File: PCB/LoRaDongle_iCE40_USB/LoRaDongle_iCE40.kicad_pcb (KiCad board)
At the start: 4 copper layers, 95 x 67 mm, 137 parts, among them IC1 93LC56BT-I_OT, IC2 ICE40UP5K-UWG30ITR1K, IC3 SGP40-D-R4, J1 USB_A, J2 Conn_01x08, J3 Conn_01x08_Male, J4 Conn_01x04_Male, J5 142-0701-801, J6 Conn_02x02_Top_Bottom, J7 Conn_01x03_Male, J8 Jumper_2_Open, SW1 SW_Push, SW2 SW_Push, U1 RP550K001A-TR, U2 FT2232HL, U3 SX1261IMLTRT, U4 SKY13587-378LF, U5 W25Q128JVS, X1 ECS-2520MV-500-BL-TR, Y1 Crystal_GND24_Small, Y2 Crystal_GND24

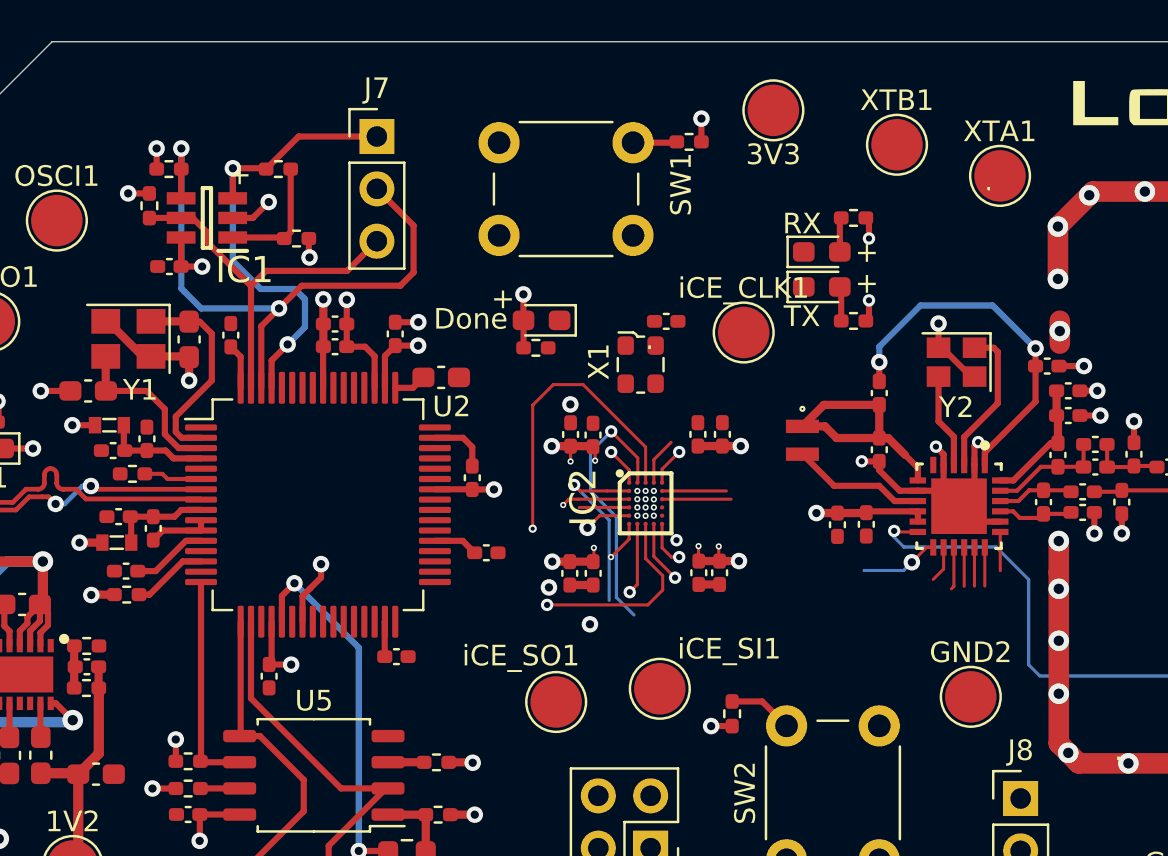
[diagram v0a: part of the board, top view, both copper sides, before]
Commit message: updated schematic to QFN ice40
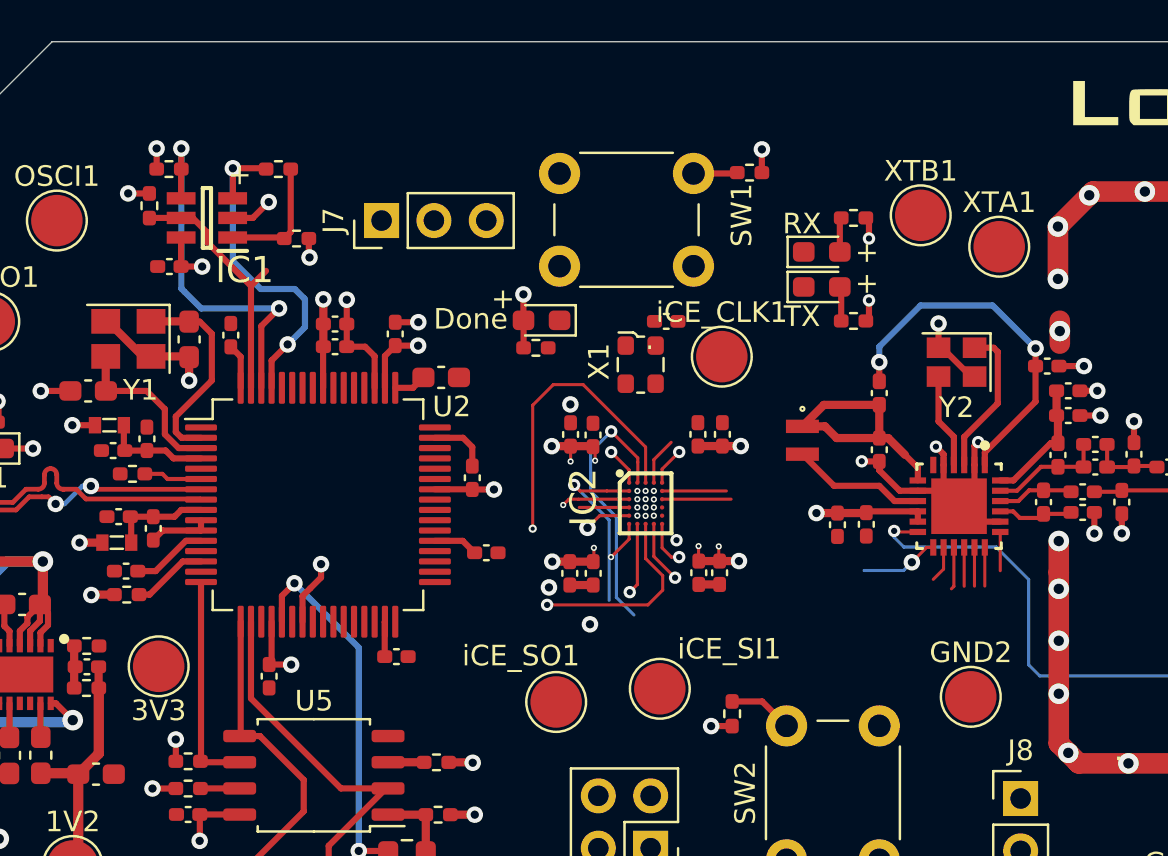
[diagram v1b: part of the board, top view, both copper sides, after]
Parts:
- moved 3V3 40.2 mm to (120.2, 105.3)
- moved J7 4.08 mm to (131.0, 83.7), turned to 90 degrees
- moved XTB1 3.61 mm to (157.2, 83.4)
- moved XTA1 3.44 mm to (161.0, 84.9)
- moved R13 3.29 mm to (148.8, 81.4)
- moved SW1 3.29 mm to (139.6, 81.4)
- moved iCE_CLK1 1.58 mm to (147.5, 90.3)
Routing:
- net /USB_Interface/CLK: track 30.6 -> 18.6 mm
- net /USB_Interface/DATA: track 22.9 -> 16.8 mm
- net Net-(IC1-Pad5): track 18.5 -> 12.6 mm

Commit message: updated routing
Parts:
- removed IC2: ICE40UP5K-UWG30ITR1K, ICE40UP5K-UWG30ITR1K_KiCad:BGA30C40P5X6_211X254X60
- added C56: 1uF, Capacitor_SMD:C_0402_1005Metric_Pad0.74x0.62mm_HandSolder, F.Cu at (137.5, 95.2)
- added C57: 100nF, Capacitor_SMD:C_0402_1005Metric_Pad0.74x0.62mm_HandSolder, F.Cu at (150.9, 97.3)
- added J9: Conn_01x17_Male, Connector_PinHeader_2.54mm:PinHeader_1x17_P2.54mm_Vertical, F.Cu at (118.1, 77.6)
- added U6: ICE40UP5K-SG48ITR, Package_DFN_QFN:QFN-48-1EP_7x7mm_P0.5mm_EP5.6x5.6mm, F.Cu at (143.8, 97.2)
- J2: value Conn_01x08 -> Conn_01x10_Male; footprint Connector_PinHeader_2.54mm:PinHeader_2x04_P2.54mm_Vertical -> Connector_PinHeader_2.54mm:PinHeader_2x05_P2.54mm_Vertical
- R12: value 4K7 -> 2k2
- moved iCE_SI1 25.4 mm to (121.0, 116.1)
- moved D2 17.9 mm to (140.3, 106.4)
- moved R12 17.9 mm to (140.0, 107.7)
- moved C26 13.7 mm to (148.7, 90.1), turned to -90 degrees
- moved iCE_CLK1 10.8 mm to (137.0, 87.6)
- moved C25 10.1 mm to (139.9, 90.8), turned to -90 degrees
- moved iCE_SO1 9.92 mm to (138.1, 116.9)
- moved C31 6.42 mm to (150.9, 99.5), turned to 180 degrees
- moved C30 6.26 mm to (150.9, 98.3), turned to 180 degrees
- moved XTA1 3.75 mm to (162.2, 81.4)
- moved C29 3.72 mm to (137.5, 94.2), turned to 180 degrees
- moved XTB1 2.85 mm to (159.5, 85.0)
- moved C28 2.79 mm to (137.6, 93.1), turned to 180 degrees
- moved R20 2.75 mm to (155.8, 86.6)
- moved R21 2.75 mm to (155.8, 81.6)
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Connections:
- net Net-(IC1-Pad5) renamed /USB_Interface/CS#
- net Net-(R14-Pad2) renamed /ice40up5k_circuit/FLASH_~{WP}
- net Net-(R16-Pad2) renamed /ice40up5k_circuit/FLASH_~{HOLD}
- J2 pad 6: GND -> /SPI_SS
- J2 pad 7: /SPI_SS -> /UART_RX
- J2 pad 8: +5V -> /UART_TX
- U2 pad 38: /USB_Interface/UART_USB_TX -> /UART_RX
- U2 pad 39: /USB_Interface/UART_USB_RX -> /UART_TX
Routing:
- net 1V2FPGA: track 12.2 -> 70.2 mm, vias 6 -> 2
- net /ice40up5k_circuit/Pin16: track 0.00 -> 49.2 mm, vias 0 -> 1
- net 3V3FPGA: track 34.3 -> 82.1 mm, vias 9 -> 3
- net /ice40up5k_circuit/Pin3: track 0.00 -> 40.1 mm, vias 0 -> 1
- net /ice40up5k_circuit/Pin2: track 0.00 -> 39.4 mm, vias 0 -> 1
- net /ice40up5k_circuit/Pin1: track 0.00 -> 38.6 mm, vias 0 -> 1
- net /ice40up5k_circuit/i2C_SDA: track 4.37 -> 40.4 mm
- net /ice40up5k_circuit/Pin15: track 0.00 -> 34.1 mm, vias 0 -> 1
- net /RF Circuitry/ANT_SW: track 2.31 -> 35.7 mm, vias 0 -> 2
- net /ice40up5k_circuit/Pin17: track 0.00 -> 33.0 mm, vias 0 -> 1
- net /ice40up5k_circuit/Pin14: track 0.00 -> 31.6 mm, vias 0 -> 1
- net 1V2: track 12.0 -> 43.0 mm
- net /ice40up5k_circuit/i2C_SCL: track 4.30 -> 34.1 mm
- net /ice40up5k_circuit/iCE_SI: track 2.26 -> 29.2 mm, vias 1 -> 2
- net /ice40up5k_circuit/iCE_SO: track 3.37 -> 30.1 mm
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
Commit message: routing complete
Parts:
- added 5V1: 5V, TestPoint:TestPoint_Pad_D2.5mm, F.Cu at (106.6, 108.1)
- moved GND1 32.1 mm to (139.2, 126.1)
- moved G3 2.99 mm to (176.1, 117.1)
- moved G2 1.25 mm to (186.2, 117.0)
- moved 3V3 0.15 mm to (120.0, 105.3)
- moved C41 0.14 mm to (176.8, 92.9)
- moved C43 0.14 mm to (176.8, 99.3)
- moved CTL2 0.09 mm to (175.6, 112.4)
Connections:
- J3 pad 5: /RF Circuitry/BUSY -> /RF Circuitry/ANT_SW
- J3 pad 7: /RF Circuitry/DIO1 -> /RF Circuitry/BUSY
- J3 pad 8: /RF Circuitry/ANT_SW -> /RF Circuitry/DIO1
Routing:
- net +5V: track 32.9 -> 100.1 mm
- net /ICE_CRESET: track 17.7 -> 80.8 mm, vias 2 -> 5
- net /RF Circuitry/ANT_SW: track 35.7 -> 85.1 mm, vias 2 -> 3
- net /UART_TX: track 7.53 -> 55.7 mm
- net /RF Circuitry/DIO1: track 15.8 -> 62.8 mm, vias 2 -> 3
- net /RF Circuitry/BUSY: track 15.3 -> 58.0 mm
- net /RF Circuitry/~{RESET}: track 15.6 -> 57.4 mm, vias 2 -> 3
- net /UART_RX: track 7.48 -> 48.6 mm, vias 0 -> 4
- net /RF Circuitry/LoRa_!SS: track 19.9 -> 57.0 mm, vias 0 -> 1
- net /RF Circuitry/LoRa_MOSI: track 15.9 -> 51.4 mm, vias 0 -> 2
- net /RF Circuitry/LoRa_MISO: track 15.2 -> 50.0 mm, vias 0 -> 1
- net /ICE_CDONE: track 28.1 -> 61.3 mm, vias 3 -> 6
- net /RF Circuitry/LoRa_SCK: track 16.8 -> 49.4 mm, vias 0 -> 1
- net 1V8: track 7.53 -> 38.6 mm
- net /SPI_SCK: track 34.6 -> 65.2 mm, vias 2 -> 3
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- added copper zone on In2.Cu, net 3V3
- added copper zone on B.Cu, net GND
- added copper zone on F.Cu, net GND
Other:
- board text added: "CPU_RESET"
- board text added: "FTDI EEPROM"
- board text added: "Gas Sensor"
- board text added: "LoRa Connector"
- board text added: "PWR"
- board text added: "RESET"
- board text removed: "FLASH"
- board text removed: "FPGA"
- board text removed: "GND"
- board text removed: "OSC"
- board text removed: "Vin"

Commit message: updated BOM
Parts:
- removed G2: LOGO, Logo:rev1.0
- added G***: LOGO, Logo:rev2, F.Cu at (186.2, 117.0)

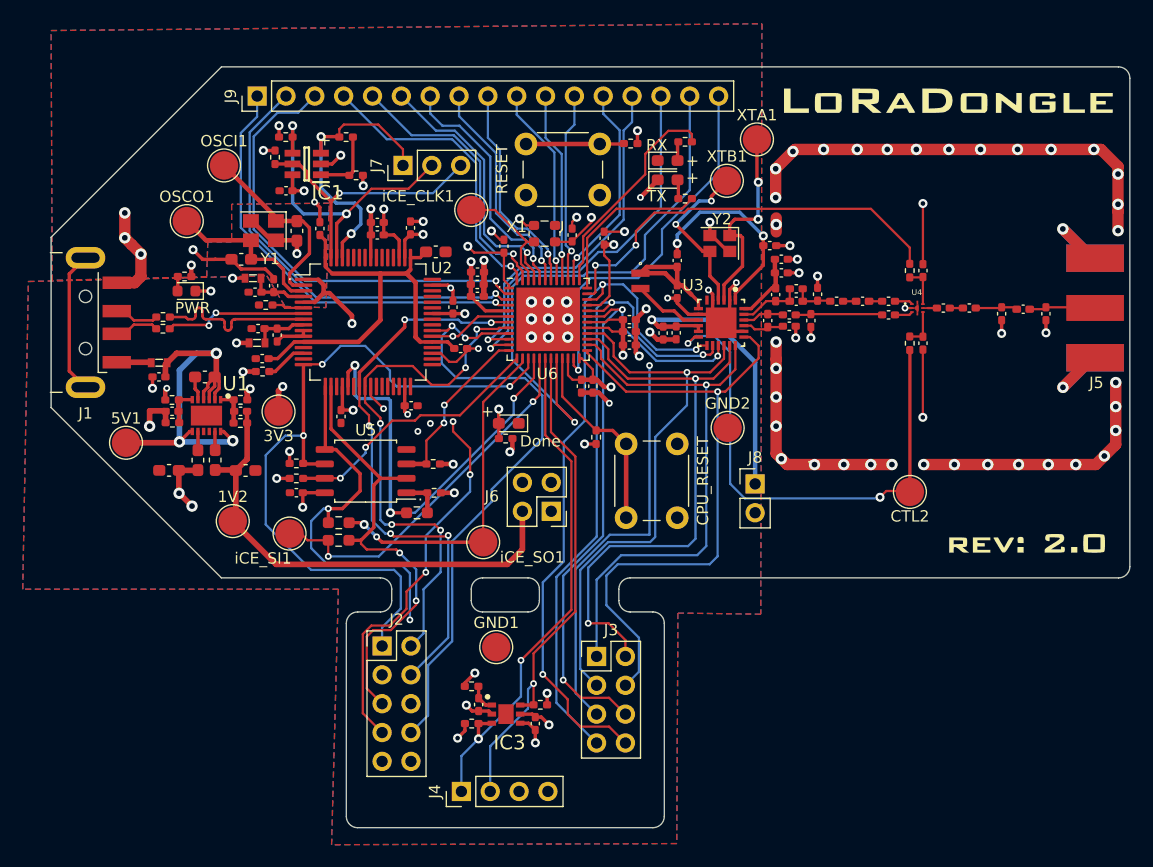
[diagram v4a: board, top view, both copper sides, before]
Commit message: updated silkscreen
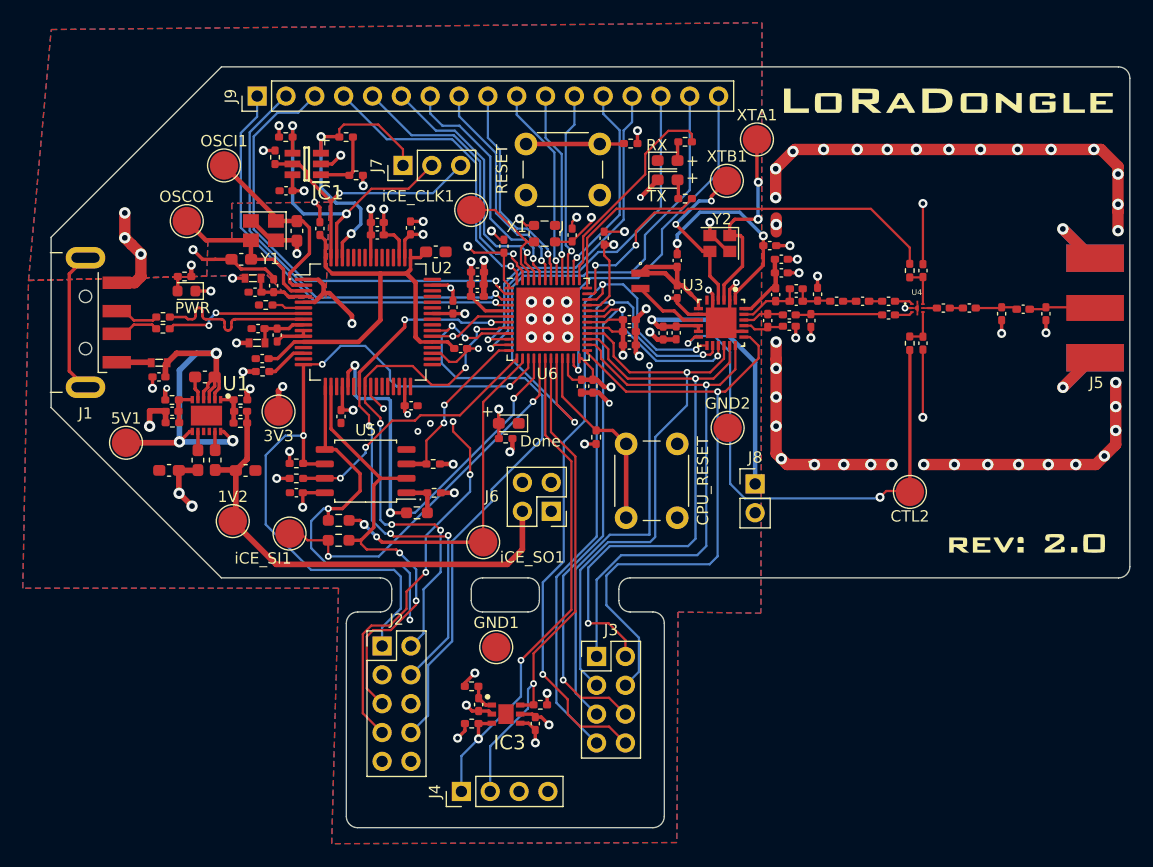
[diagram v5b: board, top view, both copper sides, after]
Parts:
- added G***: LOGO, Logo:qr_code, B.Cu at (176.5, 89.5)
- added REF**: KiCad-Logo2_5mm_SilkScreen, Symbol:KiCad-Logo2_5mm_SilkScreen, B.Cu at (182.5, 104.6)
- added REF**: OSHW-Logo2_9.8x8mm_SilkScreen, Symbol:OSHW-Logo2_9.8x8mm_SilkScreen, B.Cu at (169.2, 104.5)
- moved JP2 0.20 mm to (125.3, 114.9)

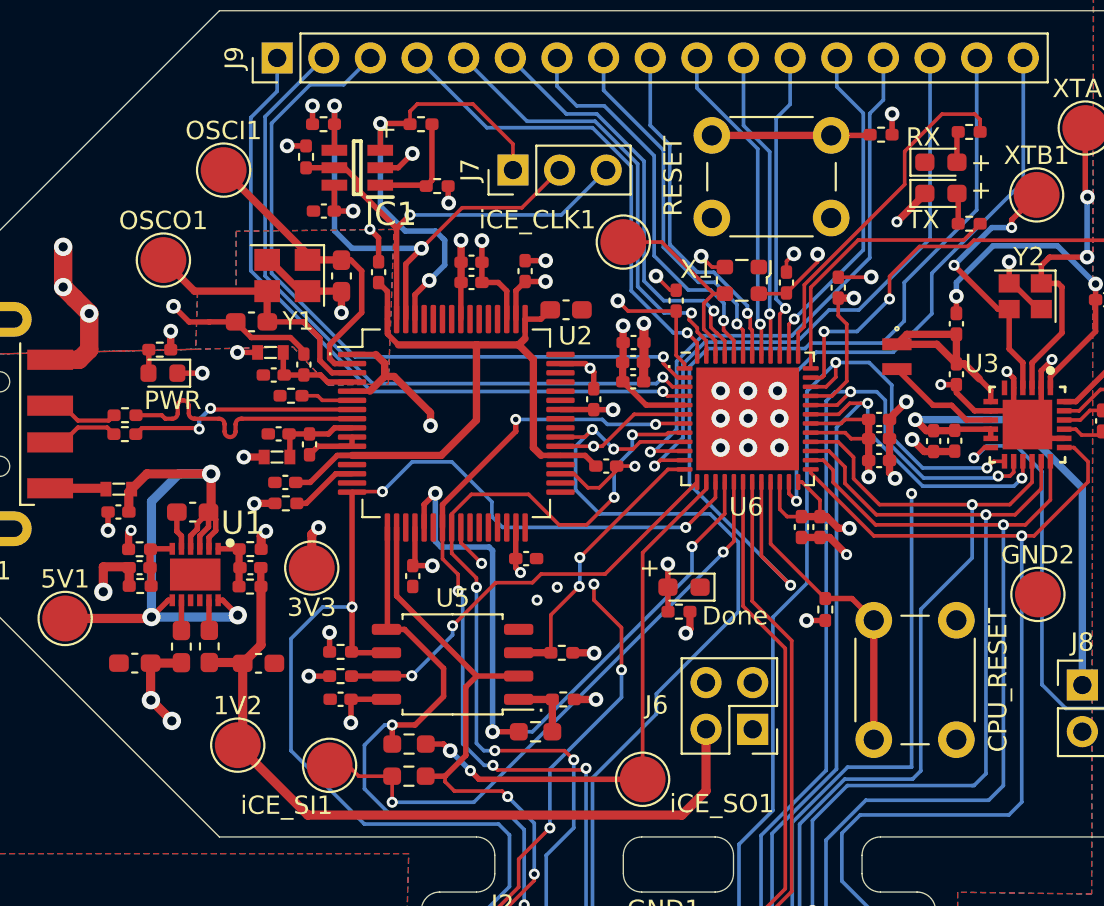
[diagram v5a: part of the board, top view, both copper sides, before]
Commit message: updated silkscreen
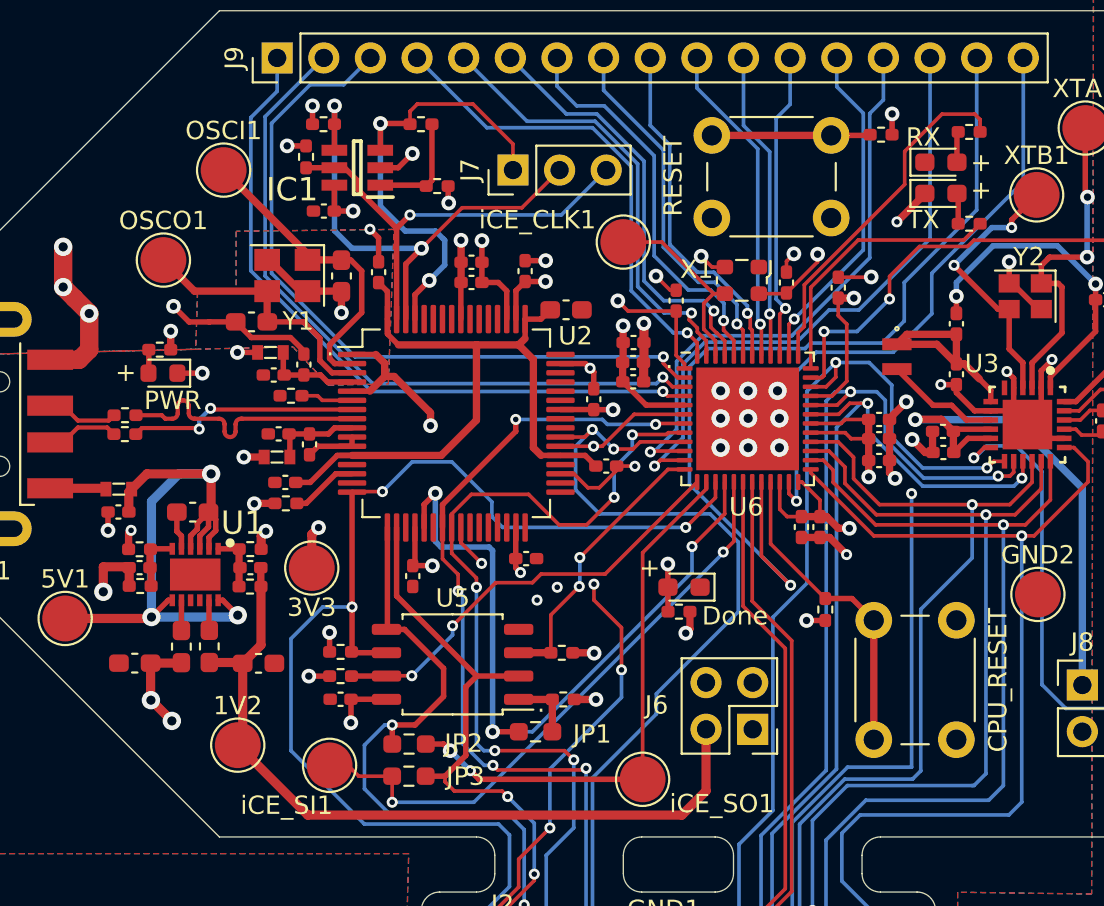
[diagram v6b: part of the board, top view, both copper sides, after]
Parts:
- moved C33 0.89 mm to (154.4, 99.1), turned to 0 degrees
- moved C34 0.74 mm to (154.4, 97.9), turned to 0 degrees
- moved REF** 0.38 mm to (169.3, 104.9)
- moved REF** 0.18 mm to (182.6, 104.8)
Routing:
- net RadioPower: track 26.3 -> 29.3 mm

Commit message: added license
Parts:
- added G***: LOGO, Logo:license2, B.Cu at (177.8, 78.8)
